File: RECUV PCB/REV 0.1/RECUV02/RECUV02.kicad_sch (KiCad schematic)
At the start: 35 parts, among them P1 VEXT, Q1 MMBT2222ALT1, Q2 MMBT2222ALT1, U1 ESP32-S3-WROOM-1, U2 CH340C, U3 A1117-3.3, U4 RESET, U5 BOOT

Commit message: Finished Microcontroller section
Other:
- note added: "AIR_HUMIDITY"
- note added: "CLOCK_1"
- note added: "CLOCK_2"
- note added: "CURRENT"
- note added: "HUMIDITY_SOIL"
- note added: "NET_WEIGHT1"
- note added: "NET_WEIGHT2"
- note added: "PLUV1"
- note added: "PLUV2"
- note added: "PLUV3"
- note added: "SCL_1"
- note added: "SCL_2"
- note added: "SDA_1"
- note added: "SDA_2"
- note added: "SOLAR_RADIATION"
- note added: "TEMP_SOIL"
- note added: "VOLTAGE"
- note added: "W_DIR01"
- note added: "W_SPEED"
- moved on the sheet: C10, C11, C12, R10, U1

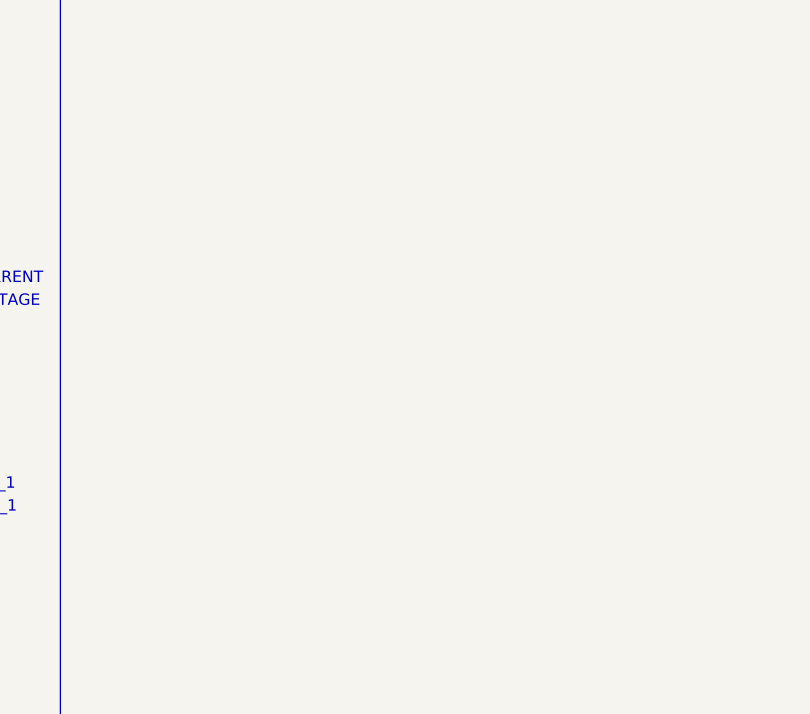
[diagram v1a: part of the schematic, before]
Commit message: Added voltage divider
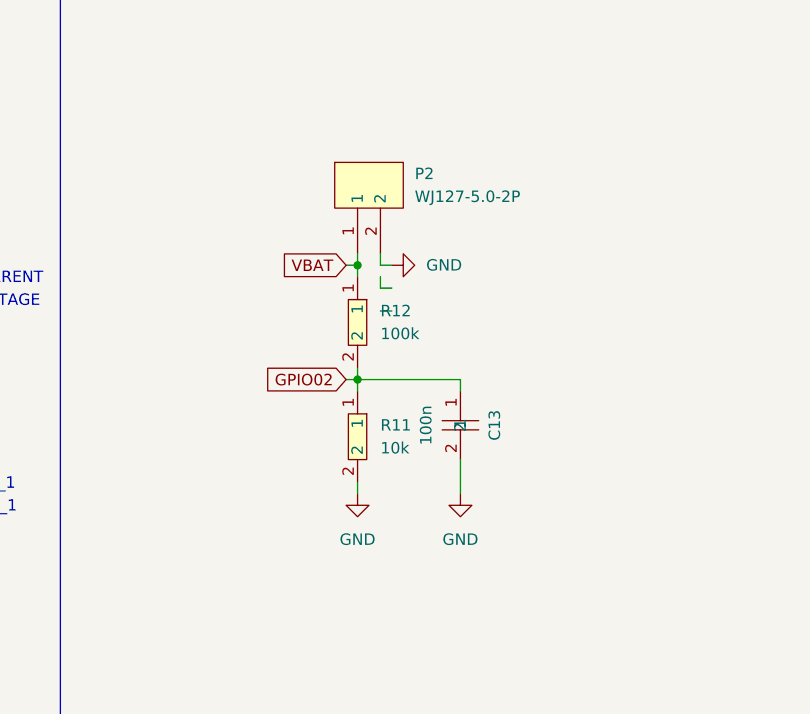
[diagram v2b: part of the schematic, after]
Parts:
- added C13: 100n, EasyEDA:C0805, symbol EasyEDA:CL21B104KBCNNNC
- added P2: WJ127-5.0-2P, EasyEDA:CONN-TH_2P-P5.00_CPC3703CTR, symbol EasyEDA:WJ127-5.0-2P
- added R11: 10k, EasyEDA:R0805, symbol EasyEDA:0805W8F1002T5E
- added R12: 100k, EasyEDA:R0805, symbol EasyEDA:0805W8J0104T5E
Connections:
- net GND: now also C13.2, P2.2, R11.2
- net GPIO02: now also C13.1, R11.1, R12.2
- new net VBAT: P2.1, R12.1

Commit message: Finished electrical sensors
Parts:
- added C14: 1n, EasyEDA:C0805, symbol EasyEDA:CL21C102JBCNNNC
- added C15: 100n, EasyEDA:C0805, symbol EasyEDA:CL21B104KBCNNNC
- added P3: CURRENT, EasyEDA:CONN-TH_2P-P5.00_CPC3703CTR, symbol EasyEDA:WJ127-5.0-2P
- added U6: ACS712ELCTR-20A-T, EasyEDA:SOIC-8_L4.9-W3.9-P1.27-LS6.0-BL, symbol EasyEDA:ACS712ELCTR-20A-T
- P2: value WJ127-5.0-2P -> VOLTAGE
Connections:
- net +5V: now also C15.1, U6.8 (VCC)
- net GND: now also C14.2, C15.2, U6.5 (GND)
- net GPIO01: now also U6.7 (VIOUT)
- new net: P3.2, U6.1 (IP+), U6.2 (IP+)
- new net: P3.1, U6.3 (IP-), U6.4 (IP-)
- new net: C14.1, U6.6 (FILTER)
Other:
- moved on the sheet: C10, C11, C12, C13, P2, R10, R11, R12, U1

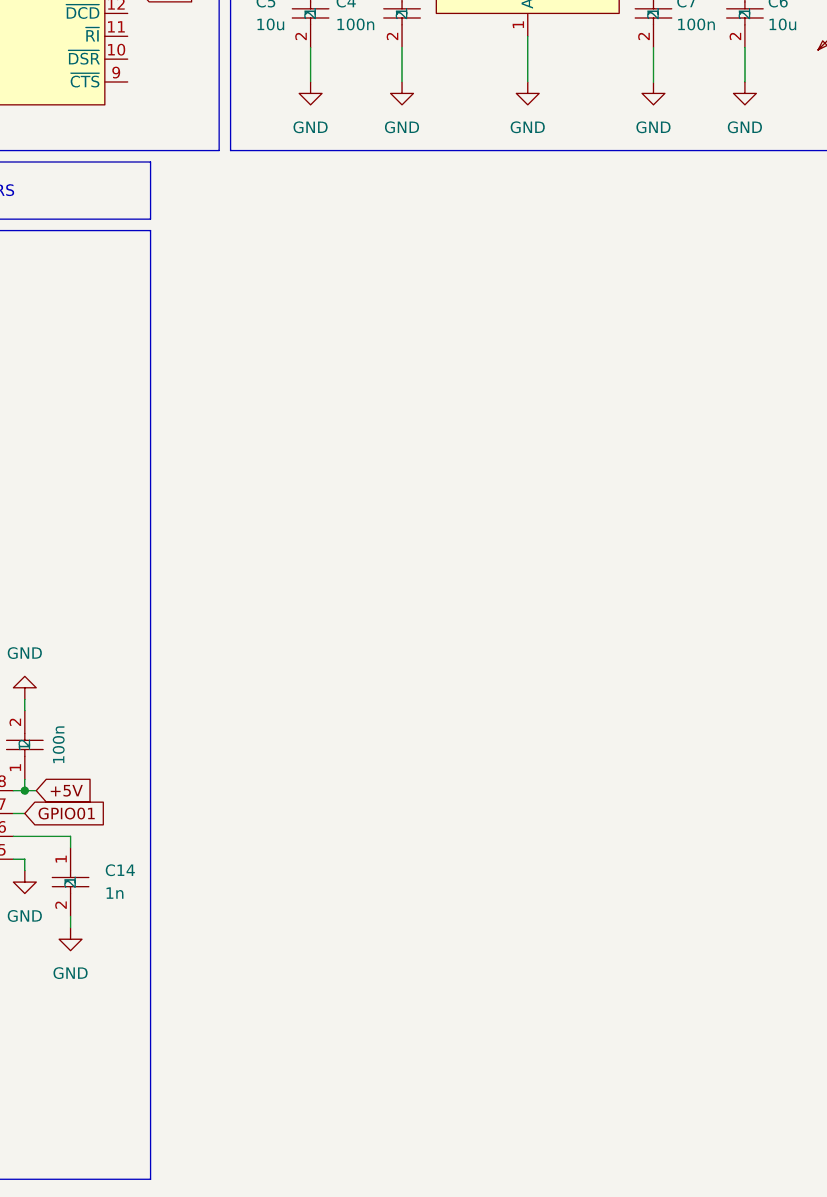
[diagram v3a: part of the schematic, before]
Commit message: Finished Bus I2C
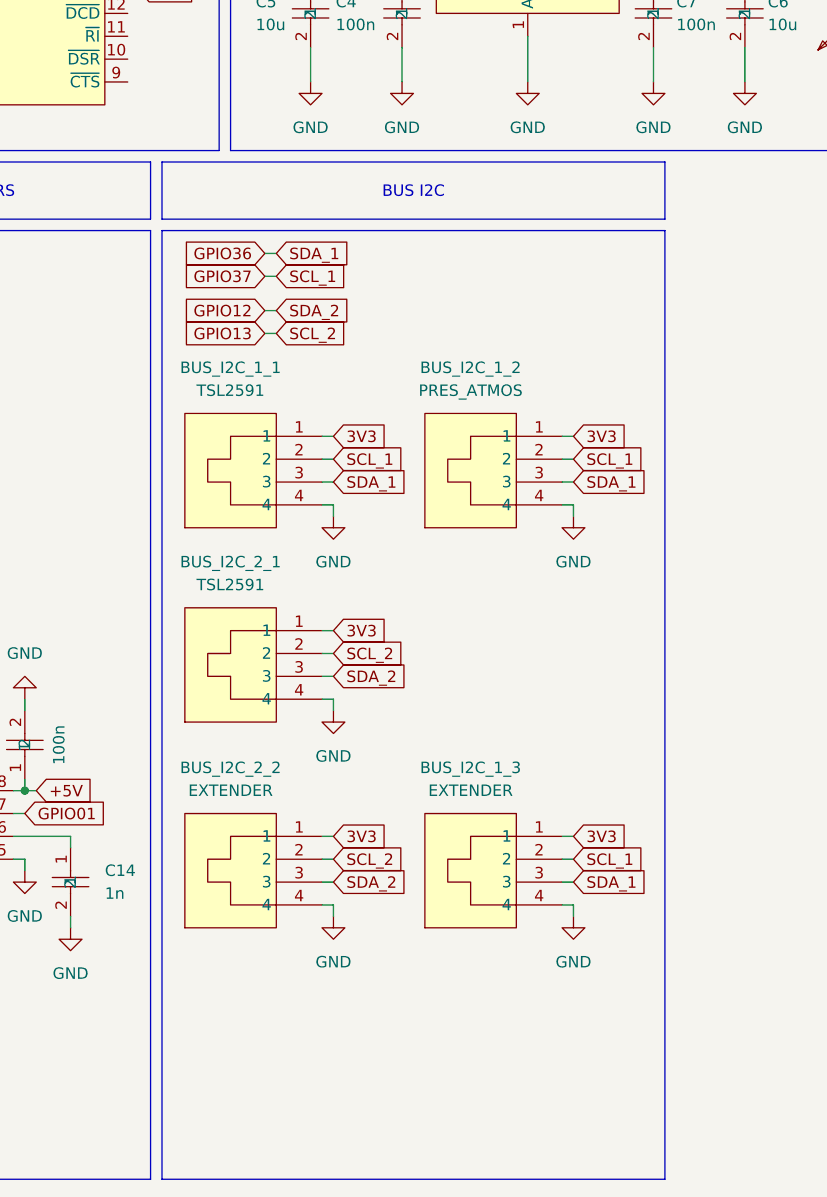
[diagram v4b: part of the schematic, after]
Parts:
- added BUS_I2C_1_1, BUS_I2C_2_1: TSL2591, EasyEDA:RJ11-TH_PCB-6P4C-90, symbol EasyEDA:PCB-6P4C-90
- added BUS_I2C_1_2: PRES_ATMOS, EasyEDA:RJ11-TH_PCB-6P4C-90, symbol EasyEDA:PCB-6P4C-90
- added BUS_I2C_1_3, BUS_I2C_2_2: EXTENDER, EasyEDA:RJ11-TH_PCB-6P4C-90, symbol EasyEDA:PCB-6P4C-90
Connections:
- net 3V3: now also BUS_I2C_1_1.1, BUS_I2C_1_2.1, BUS_I2C_1_3.1, BUS_I2C_2_1.1, BUS_I2C_2_2.1
- net GND: now also BUS_I2C_1_1.4, BUS_I2C_1_2.4, BUS_I2C_1_3.4, BUS_I2C_2_1.4, BUS_I2C_2_2.4
- net GPIO12: now also BUS_I2C_2_1.3, BUS_I2C_2_2.3
- net GPIO13: now also BUS_I2C_2_1.2, BUS_I2C_2_2.2
- net GPIO36: now also BUS_I2C_1_1.3, BUS_I2C_1_2.3, BUS_I2C_1_3.3
- net GPIO37: now also BUS_I2C_1_1.2, BUS_I2C_1_2.2, BUS_I2C_1_3.2

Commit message: Finished RJ11 sensors and corrected bus i2c bug
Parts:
- added C16, C17, C18, C19: 100n, EasyEDA:C0805, symbol EasyEDA:CL21B104KBCNNNC
- added DAVIS6450_1: SOLAR_RADIATION, EasyEDA:RJ11-TH_PCB-6P4C-90, symbol EasyEDA:PCB-6P4C-90
- added DHT22_1: AIR_HUMIDITY/AIR_TEMPERATURE, EasyEDA:RJ11-TH_PCB-6P4C-90, symbol EasyEDA:PCB-6P4C-90
- added DS18B20_1: TEMP_SOIL, EasyEDA:RJ11-TH_PCB-6P4C-90, symbol EasyEDA:PCB-6P4C-90
- added FC28_1: HUMIDITY_SOIL, EasyEDA:RJ11-TH_PCB-6P4C-90, symbol EasyEDA:PCB-6P4C-90
- added HX711_1, HX711_2: NET_WEIGHT, EasyEDA:RJ11-TH_PCB-6P4C-90, symbol EasyEDA:PCB-6P4C-90
- added PLUVIOMETER_1, PLUVIOMETER_2, PLUVIOMETER_3: PLUVIOMETER, EasyEDA:RJ11-TH_PCB-6P4C-90, symbol EasyEDA:PCB-6P4C-90
- added R13: 10k, EasyEDA:R0805, symbol EasyEDA:0805W8F1002T5E
- added R14: 2.2k, EasyEDA:R0603, symbol EasyEDA:0603WAF2201T5E
- added W_SPEED_1/W_DIR_1: WIND, EasyEDA:RJ11-TH_PCB-6P4C-90, symbol EasyEDA:PCB-6P4C-90
- BUS_I2C_1_2: value PRES_ATMOS -> TSL2591
- BUS_I2C_1_3, BUS_I2C_2_2: value EXTENDER -> TSL2591
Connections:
- net 3V3: now also BUS_I2C_1_1.4, BUS_I2C_1_2.4, BUS_I2C_1_3.4, BUS_I2C_2_1.4, BUS_I2C_2_2.4, DAVIS6450_1.4, DHT22_1.4, DS18B20_1.4, FC28_1.4, HX711_1.4, HX711_2.4, PLUVIOMETER_1.4, PLUVIOMETER_2.4, PLUVIOMETER_3.4, R13.1, R14.1; no longer BUS_I2C_1_1.1, BUS_I2C_1_2.1, BUS_I2C_1_3.1, BUS_I2C_2_1.1, BUS_I2C_2_2.1
- net GND: now also BUS_I2C_1_1.1, BUS_I2C_1_2.1, BUS_I2C_1_3.1, BUS_I2C_2_1.1, BUS_I2C_2_2.1, C16.2, C17.2, C18.2, C19.2, DAVIS6450_1.1, DAVIS6450_1.2, DHT22_1.1, DHT22_1.2, DS18B20_1.1, DS18B20_1.2, FC28_1.1, FC28_1.2, HX711_1.1, HX711_2.1, PLUVIOMETER_1.1, PLUVIOMETER_2.1, PLUVIOMETER_3.1, W_SPEED_1/W_DIR_1.1; no longer BUS_I2C_1_1.4, BUS_I2C_1_2.4, BUS_I2C_1_3.4, BUS_I2C_2_1.4, BUS_I2C_2_2.4
- net GPIO03: now also HX711_1.3
- net GPIO04: now also W_SPEED_1/W_DIR_1.3
- net GPIO05: now also R13.2, W_SPEED_1/W_DIR_1.4
- net GPIO06: now also PLUVIOMETER_1.3
- net GPIO07: now also FC28_1.3
- net GPIO08: now also PLUVIOMETER_3.3
- net GPIO09: now also HX711_1.2
- net GPIO10: now also HX711_2.3
- net GPIO11: now also HX711_2.2
- net GPIO12: now also BUS_I2C_2_1.2, BUS_I2C_2_2.2; no longer BUS_I2C_2_1.3, BUS_I2C_2_2.3
- net GPIO13: now also BUS_I2C_2_1.3, BUS_I2C_2_2.3; no longer BUS_I2C_2_1.2, BUS_I2C_2_2.2
- net GPIO15: now also DS18B20_1.3, R14.2
- net GPIO16: now also DAVIS6450_1.3
- net GPIO17: now also DHT22_1.3
- net GPIO18: now also PLUVIOMETER_2.3
- net GPIO36: now also BUS_I2C_1_1.2, BUS_I2C_1_2.2, BUS_I2C_1_3.2; no longer BUS_I2C_1_1.3, BUS_I2C_1_2.3, BUS_I2C_1_3.3
- net GPIO37: now also BUS_I2C_1_1.3, BUS_I2C_1_2.3, BUS_I2C_1_3.3; no longer BUS_I2C_1_1.2, BUS_I2C_1_2.2, BUS_I2C_1_3.2
- new net: C16.1, W_SPEED_1/W_DIR_1.2
- new net: C19.1, PLUVIOMETER_3.2
- new net: C18.1, PLUVIOMETER_2.2
- new net: C17.1, PLUVIOMETER_1.2
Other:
- note added: "W_DIR"
- note removed: "W_DIR01"

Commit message: Finished all PCB sections
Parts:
- added H1: LEFT_ROW_2, EasyEDA:HDR-TH_6P-P2.54-V-M-1, symbol EasyEDA:Header-Male-2.54_1x6
- added H2: LOW_ROW, EasyEDA:HDR-TH_10P-P2.54-V-M-1, symbol EasyEDA:Header-Male-2.54_1x10
- added H3: RIGHT_ROW_1, EasyEDA:HDR-TH_6P-P2.54-V-M-1, symbol EasyEDA:Header-Male-2.54_1x6
- added H4: RIGHT_ROW_2, EasyEDA:HDR-TH_6P-P2.54-V-M-1, symbol EasyEDA:Header-Male-2.54_1x6
- added P4: LEFT_ROW_1, EasyEDA:HDR-TH_3P-P1.27-V-M-1, symbol EasyEDA:1.27mm_1*3p
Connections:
- net GPIO01: now also H3.1
- net GPIO02: now also H3.2
- net GPIO03: now also H2.1
- net GPIO04: now also P4.1
- net GPIO05: now also P4.2
- net GPIO06: now also P4.3
- net GPIO07: now also H1.1
- net GPIO08: now also H1.6
- net GPIO09: now also H2.2
- net GPIO10: now also H2.3
- net GPIO11: now also H2.4
- net GPIO12: now also H2.5
- net GPIO13: now also H2.6
- net GPIO14: now also H2.7
- net GPIO15: now also H1.2
- net GPIO16: now also H1.3
- net GPIO17: now also H1.4
- net GPIO18: now also H1.5
- net GPIO21: now also H2.8
- net GPIO35: now also H4.6
- net GPIO36: now also H4.5
- net GPIO37: now also H4.4
- net GPIO38: now also H4.3
- net GPIO39: now also H4.2
- net GPIO40: now also H4.1
- net GPIO41: now also H3.6
- net GPIO42: now also H3.5
- net GPIO47: now also H2.9
- net GPIO48: now also H2.10
- net U0RXD: now also H3.4
- net U0TXD: now also H3.3

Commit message: Finished PCB
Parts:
- removed P4: LEFT_ROW_1, EasyEDA:HDR-TH_3P-P1.27-V-M-1, symbol EasyEDA:1.27mm_1*3p
- added H5: LEFT_ROW_1, EasyEDA:HDR-TH_3P-P2.54-V-M, symbol EasyEDA:A2541WV-3P_C5445396
- added H6: 5V_ROW, EasyEDA:HDR-TH_3P-P2.54-V-M, symbol EasyEDA:A2541WV-3P_C5445396
- added H7: 3V3_ROW, EasyEDA:HDR-TH_3P-P2.54-V-M, symbol EasyEDA:A2541WV-3P_C5445396
- added H8: GND_ROW, EasyEDA:HDR-TH_3P-P2.54-V-M, symbol EasyEDA:A2541WV-3P_C5445396
- added UART_1: COMMUNICATION, EasyEDA:RJ11-TH_PCB-6P4C-90, symbol EasyEDA:PCB-6P4C-90
- BUS_I2C_1_2: value TSL2591 -> PRES_ATMOS
- BUS_I2C_1_3, BUS_I2C_2_2: value TSL2591 -> EXTENDER
- USB1: footprint EasyEDA:USB-TYPE-C-TH_USB-306. -> EasyEDA:USB-TYPE-C-TH_USB-306-1
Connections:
- net +5V: now also H6.1, H6.2, H6.3, UART_1.4
- net 3V3: now also H7.1, H7.2, H7.3
- net GND: now also H8.1, H8.2, H8.3, UART_1.1
- net GPIO04: now also H5.1
- net GPIO05: now also H5.2
- net GPIO06: now also H5.3
- net GPIO14: now also UART_1.3
- net GPIO21: now also UART_1.2
- net at U6.1 (IP+), U6.2 (IP+): now also P3.1; no longer P3.2
- net at U6.3 (IP-), U6.4 (IP-): now also P3.2; no longer P3.1
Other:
- note added: "RX_1"
- note added: "TX_1"
